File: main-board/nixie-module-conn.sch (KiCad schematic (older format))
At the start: 3 parts, among them P3 CONN_02X05, P4 CONN_02X05, U4 PCF8574

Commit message: #1 - zmiana wartosci kondensator do typuszeregu, usuniecie D2, UF4004 na D4, przyciagniecie do masy bramki Q1, bezpiecznik na wejsciu przetwornicy, gniazdo IEC C7, 100n na zasilaniu PCF8574
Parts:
- added C?: 100n, symbol C
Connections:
- wire segments 60 -> 62
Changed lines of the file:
@@
 $Descr A4 11693 8268
 encoding utf-8
-Sheet 4 4
+Sheet 3 4
 Title ""
 Date ""
@@
 Wire Wire Line
 	3550 3150 3550 2550
+$Comp
+L C C?
+U 1 1 582C0EF1
+P 4850 3000
+F 0 "C?" H 4875 3100 50  0000 L CNN
+F 1 "100n" H 4875 2900 50  0000 L CNN
+F 2 "" H 4888 2850 50  0000 C CNN
+F 3 "" H 4850 3000 50  0000 C CNN
+	1    4850 3000
+	1    0    0    -1
+$EndComp
+$Comp
+L GND #PWR?
+U 1 1 582C10A0
+P 4850 3200
+F 0 "#PWR?" H 4850 2950 50  0001 C CNN
+F 1 "GND" H 4850 3050 50  0000 C CNN
+F 2 "" H 4850 3200 50  0000 C CNN
+F 3 "" H 4850 3200 50  0000 C CNN
+	1    4850 3200
+	1    0    0    -1
+$EndComp
+Wire Wire Line
+	4850 3200 4850 3150
+Wire Wire Line
+	4850 2850 4850 2800
 $EndSCHEMATC

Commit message: #1 - stabilizator LDO AMS1117-3.3V
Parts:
- gave numbers to parts that had none: 1
- renumbered P3 to P4, P4 to P5, U4 to U5
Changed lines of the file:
@@
 $EndDescr
 $Comp
-L PCF8574 U4
+L PCF8574 U5
 U 1 1 58191F22
 P 5550 3800
-AR Path="/581979CF/58191F22" Ref="U4"  Part="1"
-AR Path="/58191DB1/58191F22" Ref="U4"  Part="1"
-F 0 "U4" H 5200 4400 50  0000 L CNN
+AR Path="/58191DB1/58191F22" Ref="U5"  Part="1"
+AR Path="/581979CF/58191F22" Ref="U6"  Part="1"
+F 0 "U5" H 5200 4400 50  0000 L CNN
 F 1 "PCF8574" H 5650 4400 50  0000 L CNN
 F 2 "" H 5550 3800 50  0000 C CNN
@@
 5VDC
 $Comp
-L VDD #PWR016
+L VDD #PWR028
 U 1 1 58192F62
 P 4850 2800
-AR Path="/581979CF/58192F62" Ref="#PWR016"  Part="1"
-AR Path="/58191DB1/58192F62" Ref="#PWR016"  Part="1"
-F 0 "#PWR016" H 4850 2650 50  0001 C CNN
+AR Path="/58191DB1/58192F62" Ref="#PWR028"  Part="1"
+AR Path="/581979CF/58192F62" Ref="#PWR033"  Part="1"
+F 0 "#PWR028" H 4850 2650 50  0001 C CNN
 F 1 "VDD" H 4850 2950 50  0000 C CNN
 F 2 "" H 4850 2800 50  0000 C CNN
@@
 $EndComp
 $Comp
-L PWR_FLAG #FLG017
+L PWR_FLAG #FLG029
 U 1 1 58192F79
 P 4150 3100
-AR Path="/581979CF/58192F79" Ref="#FLG017"  Part="1"
-AR Path="/58191DB1/58192F79" Ref="#FLG017"  Part="1"
-F 0 "#FLG017" H 4150 3195 50  0001 C CNN
+AR Path="/58191DB1/58192F79" Ref="#FLG029"  Part="1"
+AR Path="/581979CF/58192F79" Ref="#FLG034"  Part="1"
+F 0 "#FLG029" H 4150 3195 50  0001 C CNN
 F 1 "PWR_FLAG" H 4150 3280 50  0000 C CNN
 F 2 "" H 4150 3100 50  0000 C CNN
@@
 GND
 $Comp
-L PWR_FLAG #FLG018
+L PWR_FLAG #FLG030
 U 1 1 581931A2
 P 4100 4350
-AR Path="/581979CF/581931A2" Ref="#FLG018"  Part="1"
-AR Path="/58191DB1/581931A2" Ref="#FLG018"  Part="1"
-F 0 "#FLG018" H 4100 4445 50  0001 C CNN
+AR Path="/58191DB1/581931A2" Ref="#FLG030"  Part="1"
+AR Path="/581979CF/581931A2" Ref="#FLG035"  Part="1"
+F 0 "#FLG030" H 4100 4445 50  0001 C CNN
 F 1 "PWR_FLAG" H 4100 4530 50  0000 C CNN
 F 2 "" H 4100 4350 50  0000 C CNN
@@
 $EndComp
 $Comp
-L GND #PWR019
+L GND #PWR031
 U 1 1 581931CA
 P 4900 4800
-AR Path="/581979CF/581931CA" Ref="#PWR019"  Part="1"
-AR Path="/58191DB1/581931CA" Ref="#PWR019"  Part="1"
-F 0 "#PWR019" H 4900 4550 50  0001 C CNN
+AR Path="/58191DB1/581931CA" Ref="#PWR031"  Part="1"
+AR Path="/581979CF/581931CA" Ref="#PWR036"  Part="1"
+F 0 "#PWR031" H 4900 4550 50  0001 C CNN
 F 1 "GND" H 4900 4650 50  0000 C CNN
 F 2 "" H 4900 4800 50  0000 C CNN
@@
 	4600 3900 5050 3900
 $Comp
-L CONN_02X05 P3
+L CONN_02X05 P4
 U 1 1 58193880
 P 7450 3300
-AR Path="/581979CF/58193880" Ref="P3"  Part="1"
-AR Path="/58191DB1/58193880" Ref="P3"  Part="1"
-F 0 "P3" H 7450 3600 50  0000 C CNN
+AR Path="/58191DB1/58193880" Ref="P4"  Part="1"
+AR Path="/581979CF/58193880" Ref="P6"  Part="1"
+F 0 "P4" H 7450 3600 50  0000 C CNN
 F 1 "CONN_02X05" H 7450 3000 50  0000 C CNN
 F 2 "" H 7450 2100 50  0000 C CNN
@@
 $EndComp
 $Comp
-L CONN_02X05 P4
+L CONN_02X05 P5
 U 1 1 581938E3
 P 7450 4350
-AR Path="/581979CF/581938E3" Ref="P4"  Part="1"
-AR Path="/58191DB1/581938E3" Ref="P4"  Part="1"
-F 0 "P4" H 7450 4650 50  0000 C CNN
+AR Path="/58191DB1/581938E3" Ref="P5"  Part="1"
+AR Path="/581979CF/581938E3" Ref="P7"  Part="1"
+F 0 "P5" H 7450 4650 50  0000 C CNN
 F 1 "CONN_02X05" H 7450 4050 50  0000 C CNN
 F 2 "" H 7450 3150 50  0000 C CNN
@@
 	3550 3150 3550 2550
 $Comp
-L C C?
+L C C18
 U 1 1 582C0EF1
 P 4850 3000
-F 0 "C?" H 4875 3100 50  0000 L CNN
+AR Path="/58191DB1/582C0EF1" Ref="C18"  Part="1"
+AR Path="/581979CF/582C0EF1" Ref="C19"  Part="1"
+F 0 "C18" H 4875 3100 50  0000 L CNN
 F 1 "100n" H 4875 2900 50  0000 L CNN
 F 2 "" H 4888 2850 50  0000 C CNN
@@
 $EndComp
 $Comp
-L GND #PWR?
+L GND #PWR032
 U 1 1 582C10A0
 P 4850 3200
-F 0 "#PWR?" H 4850 2950 50  0001 C CNN
+AR Path="/58191DB1/582C10A0" Ref="#PWR032"  Part="1"
+AR Path="/581979CF/582C10A0" Ref="#PWR037"  Part="1"
+F 0 "#PWR032" H 4850 2950 50  0001 C CNN
 F 1 "GND" H 4850 3050 50  0000 C CNN
 F 2 "" H 4850 3200 50  0000 C CNN

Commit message: Oznaczenie MOSFET-ow od I2C; pojemnosc do filtrowania wysokich czestotliwosci za przetwornica boost; obudowy wiekszosci elementow
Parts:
- C18: footprint (none) -> Capacitors_SMD:C_0805_HandSoldering
- P4, P5: footprint (none) -> Pin_Headers:Pin_Header_Straight_SMT_02x05
- U4: renamed from U5; footprint (none) -> Housings_SOIC:SOIC-16W_7.5x10.3mm_Pitch1.27mm
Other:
- note removed: "Gowniane oznaczenie\n8pin - GND"
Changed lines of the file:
@@
 $EndDescr
 $Comp
-L PCF8574 U5
+L PCF8574 U4
 U 1 1 58191F22
 P 5550 3800
-AR Path="/58191DB1/58191F22" Ref="U5"  Part="1"
-AR Path="/581979CF/58191F22" Ref="U6"  Part="1"
-F 0 "U5" H 5200 4400 50  0000 L CNN
+AR Path="/58191DB1/58191F22" Ref="U4"  Part="1"
+AR Path="/581979CF/58191F22" Ref="U5"  Part="1"
+F 0 "U4" H 5200 4400 50  0000 L CNN
 F 1 "PCF8574" H 5650 4400 50  0000 L CNN
-F 2 "" H 5550 3800 50  0000 C CNN
+F 2 "Housings_SOIC:SOIC-16W_7.5x10.3mm_Pitch1.27mm" H 5550 3800 50  0001 C CNN
 F 3 "" H 5550 3800 50  0000 C CNN
 	1    5550 3800
@@
 5VDC
 $Comp
-L VDD #PWR028
+L VDD #PWR029
 U 1 1 58192F62
 P 4850 2800
-AR Path="/58191DB1/58192F62" Ref="#PWR028"  Part="1"
-AR Path="/581979CF/58192F62" Ref="#PWR033"  Part="1"
-F 0 "#PWR028" H 4850 2650 50  0001 C CNN
+AR Path="/58191DB1/58192F62" Ref="#PWR029"  Part="1"
+AR Path="/581979CF/58192F62" Ref="#PWR034"  Part="1"
+F 0 "#PWR034" H 4850 2650 50  0001 C CNN
 F 1 "VDD" H 4850 2950 50  0000 C CNN
 F 2 "" H 4850 2800 50  0000 C CNN
@@
 $EndComp
 $Comp
-L PWR_FLAG #FLG029
+L PWR_FLAG #FLG030
 U 1 1 58192F79
 P 4150 3100
-AR Path="/58191DB1/58192F79" Ref="#FLG029"  Part="1"
-AR Path="/581979CF/58192F79" Ref="#FLG034"  Part="1"
-F 0 "#FLG029" H 4150 3195 50  0001 C CNN
+AR Path="/58191DB1/58192F79" Ref="#FLG030"  Part="1"
+AR Path="/581979CF/58192F79" Ref="#FLG035"  Part="1"
+F 0 "#FLG035" H 4150 3195 50  0001 C CNN
 F 1 "PWR_FLAG" H 4150 3280 50  0000 C CNN
 F 2 "" H 4150 3100 50  0000 C CNN
@@
 GND
 $Comp
-L PWR_FLAG #FLG030
+L PWR_FLAG #FLG031
 U 1 1 581931A2
 P 4100 4350
-AR Path="/58191DB1/581931A2" Ref="#FLG030"  Part="1"
-AR Path="/581979CF/581931A2" Ref="#FLG035"  Part="1"
-F 0 "#FLG030" H 4100 4445 50  0001 C CNN
+AR Path="/58191DB1/581931A2" Ref="#FLG031"  Part="1"
+AR Path="/581979CF/581931A2" Ref="#FLG036"  Part="1"
+F 0 "#FLG036" H 4100 4445 50  0001 C CNN
 F 1 "PWR_FLAG" H 4100 4530 50  0000 C CNN
 F 2 "" H 4100 4350 50  0000 C CNN
@@
 $EndComp
 $Comp
-L GND #PWR031
+L GND #PWR032
 U 1 1 581931CA
 P 4900 4800
-AR Path="/58191DB1/581931CA" Ref="#PWR031"  Part="1"
-AR Path="/581979CF/581931CA" Ref="#PWR036"  Part="1"
-F 0 "#PWR031" H 4900 4550 50  0001 C CNN
+AR Path="/58191DB1/581931CA" Ref="#PWR032"  Part="1"
+AR Path="/581979CF/581931CA" Ref="#PWR037"  Part="1"
+F 0 "#PWR037" H 4900 4550 50  0001 C CNN
 F 1 "GND" H 4900 4650 50  0000 C CNN
 F 2 "" H 4900 4800 50  0000 C CNN
@@
 F 0 "P4" H 7450 3600 50  0000 C CNN
 F 1 "CONN_02X05" H 7450 3000 50  0000 C CNN
-F 2 "" H 7450 2100 50  0000 C CNN
+F 2 "Pin_Headers:Pin_Header_Straight_SMT_02x05" H 7450 2100 50  0001 C CNN
 F 3 "" H 7450 2100 50  0000 C CNN
 	1    7450 3300
@@
 F 0 "P5" H 7450 4650 50  0000 C CNN
 F 1 "CONN_02X05" H 7450 4050 50  0000 C CNN
-F 2 "" H 7450 3150 50  0000 C CNN
+F 2 "Pin_Headers:Pin_Header_Straight_SMT_02x05" H 7450 3150 50  0001 C CNN
 F 3 "" H 7450 3150 50  0000 C CNN
 	1    7450 4350
@@
 Text Label 7900 3300 2    60   ~ 0
 1D
-Text Notes 5500 4650 2    60   ~ 0
-Gowniane oznaczenie\n8pin - GND
 Text Label 7000 4250 0    60   ~ 0
 2A
@@
 F 0 "C18" H 4875 3100 50  0000 L CNN
 F 1 "100n" H 4875 2900 50  0000 L CNN
-F 2 "" H 4888 2850 50  0000 C CNN
+F 2 "Capacitors_SMD:C_0805_HandSoldering" H 4888 2850 50  0001 C CNN
 F 3 "" H 4850 3000 50  0000 C CNN
 	1    4850 3000
@@
 $EndComp
 $Comp
-L GND #PWR032
+L GND #PWR033
 U 1 1 582C10A0
 P 4850 3200
-AR Path="/58191DB1/582C10A0" Ref="#PWR032"  Part="1"
-AR Path="/581979CF/582C10A0" Ref="#PWR037"  Part="1"
-F 0 "#PWR032" H 4850 2950 50  0001 C CNN
+AR Path="/58191DB1/582C10A0" Ref="#PWR033"  Part="1"
+AR Path="/581979CF/582C10A0" Ref="#PWR038"  Part="1"
+F 0 "#PWR038" H 4850 2950 50  0001 C CNN
 F 1 "GND" H 4850 3050 50  0000 C CNN
 F 2 "" H 4850 3200 50  0000 C CNN

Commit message: usunięcie błędnego połączenia VDD z +5V
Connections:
- net labels removed: VDD
- wire segments 62 -> 60
- no-connect marks 0 -> 1
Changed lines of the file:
@@
 Text HLabel 3550 3300 0    60   Input ~ 0
 5VDC
-$Comp
-L VDD #PWR029
-U 1 1 58192F62
-P 4850 2800
-AR Path="/58191DB1/58192F62" Ref="#PWR029"  Part="1"
-AR Path="/581979CF/58192F62" Ref="#PWR034"  Part="1"
-F 0 "#PWR034" H 4850 2650 50  0001 C CNN
-F 1 "VDD" H 4850 2950 50  0000 C CNN
-F 2 "" H 4850 2800 50  0000 C CNN
-F 3 "" H 4850 2800 50  0000 C CNN
-	1    4850 2800
-	1    0    0    -1
-$EndComp
-$Comp
-L PWR_FLAG #FLG030
-U 1 1 58192F79
-P 4150 3100
-AR Path="/58191DB1/58192F79" Ref="#FLG030"  Part="1"
-AR Path="/581979CF/58192F79" Ref="#FLG035"  Part="1"
-F 0 "#FLG035" H 4150 3195 50  0001 C CNN
-F 1 "PWR_FLAG" H 4150 3280 50  0000 C CNN
-F 2 "" H 4150 3100 50  0000 C CNN
-F 3 "" H 4150 3100 50  0000 C CNN
-	1    4150 3100
-	0    1    1    0
-$EndComp
-Wire Wire Line
-	3850 3100 4150 3100
 Wire Wire Line
 	3850 2800 6800 2800
@@
 Wire Wire Line
 	3850 2800 3850 3300
-Connection ~ 3850 3100
 Text HLabel 3550 4200 0    60   Input ~ 0
 GND
 $Comp
-L PWR_FLAG #FLG031
-U 1 1 581931A2
-P 4100 4350
-AR Path="/58191DB1/581931A2" Ref="#FLG031"  Part="1"
-AR Path="/581979CF/581931A2" Ref="#FLG036"  Part="1"
-F 0 "#FLG036" H 4100 4445 50  0001 C CNN
-F 1 "PWR_FLAG" H 4100 4530 50  0000 C CNN
-F 2 "" H 4100 4350 50  0000 C CNN
-F 3 "" H 4100 4350 50  0000 C CNN
-	1    4100 4350
-	0    1    1    0
-$EndComp
-$Comp
-L GND #PWR032
+L GND #PWR027
 U 1 1 581931CA
 P 4900 4800
-AR Path="/58191DB1/581931CA" Ref="#PWR032"  Part="1"
-AR Path="/581979CF/581931CA" Ref="#PWR037"  Part="1"
-F 0 "#PWR037" H 4900 4550 50  0001 C CNN
+AR Path="/58191DB1/581931CA" Ref="#PWR027"  Part="1"
+AR Path="/581979CF/581931CA" Ref="#PWR030"  Part="1"
+F 0 "#PWR027" H 4900 4550 50  0001 C CNN
 F 1 "GND" H 4900 4650 50  0000 C CNN
 F 2 "" H 4900 4800 50  0000 C CNN
@@
 $EndComp
 Wire Wire Line
-	3850 4350 4100 4350
-Wire Wire Line
 	3850 4200 3850 4700
 Wire Wire Line
@@
 Wire Wire Line
 	4900 4700 4900 4800
-Connection ~ 3850 4350
 Wire Wire Line
 	5550 4700 5550 4500
@@
 $EndComp
 $Comp
-L GND #PWR033
+L GND #PWR028
 U 1 1 582C10A0
 P 4850 3200
-AR Path="/58191DB1/582C10A0" Ref="#PWR033"  Part="1"
-AR Path="/581979CF/582C10A0" Ref="#PWR038"  Part="1"
-F 0 "#PWR038" H 4850 2950 50  0001 C CNN
+AR Path="/58191DB1/582C10A0" Ref="#PWR028"  Part="1"
+AR Path="/581979CF/582C10A0" Ref="#PWR031"  Part="1"
+F 0 "#PWR028" H 4850 2950 50  0001 C CNN
 F 1 "GND" H 4850 3050 50  0000 C CNN
 F 2 "" H 4850 3200 50  0000 C CNN
@@
 Wire Wire Line
 	4850 2850 4850 2800
+NoConn ~ 5050 4200
 $EndSCHEMATC

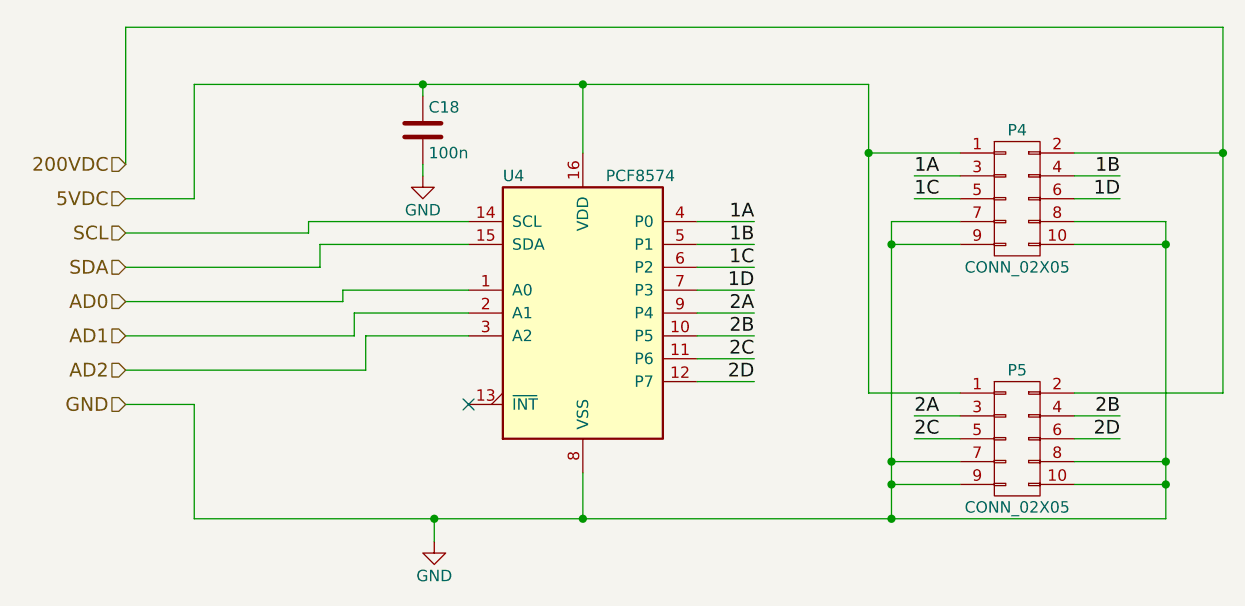
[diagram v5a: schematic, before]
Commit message: Obrys plytki 40% elementow
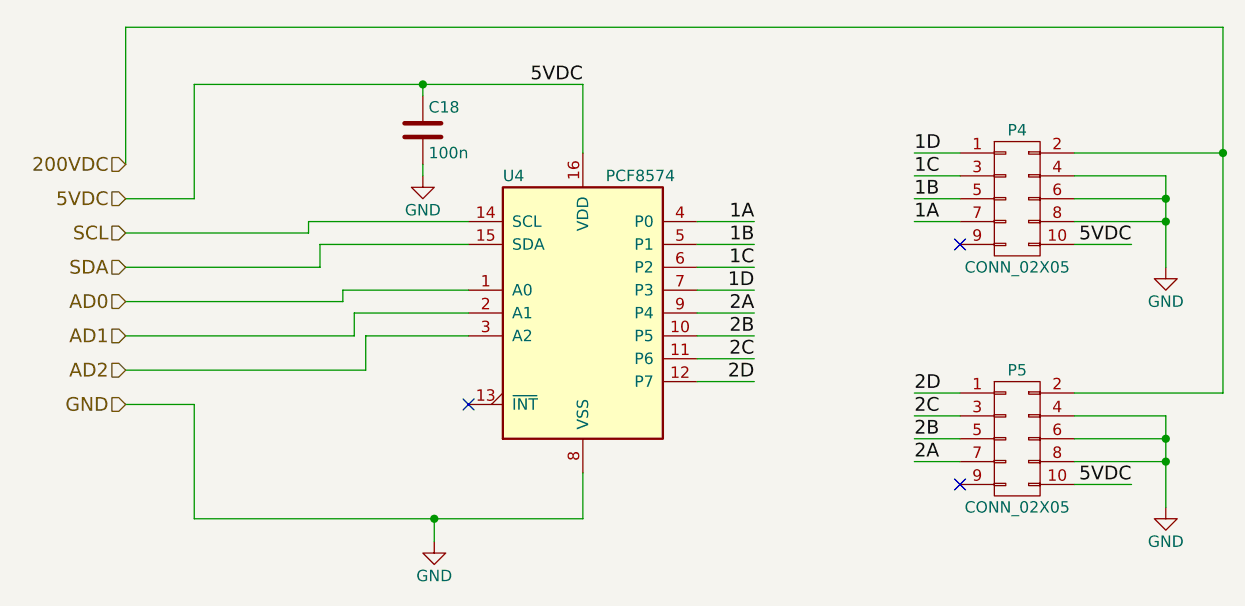
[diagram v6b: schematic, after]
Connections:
- net 1A: now also P4.7 (P7); no longer P4.3 (P3)
- net 1B: now also P4.5 (P5); no longer P4.4 (P4)
- net 1C: now also P4.3 (P3); no longer P4.5 (P5)
- net 1D: now also P4.1 (P1); no longer P4.6 (P6)
- net 2A: now also P5.7 (P7); no longer P5.3 (P3)
- net 2B: now also P5.5 (P5); no longer P5.4 (P4)
- net 2C: now also P5.3 (P3); no longer P5.5 (P5)
- net 2D: now also P5.1 (P1); no longer P5.6 (P6)
- net 5VDC: now also P4.10 (P10), P5.10 (P10); no longer P4.1 (P1), P5.1 (P1)
- net GND: now also P4.4 (P4), P4.6 (P6), P5.4 (P4), P5.6 (P6); no longer P4.10 (P10), P4.7 (P7), P4.9 (P9), P5.10 (P10), P5.7 (P7), P5.9 (P9)
- no-connect marks 1 -> 3
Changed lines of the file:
@@
 5VDC
-Wire Wire Line
-	3850 2800 6800 2800
 Wire Wire Line
 	5550 2800 5550 3100
-Connection ~ 4850 2800
 Wire Wire Line
 	3850 2800 3850 3300
@@
 GND
 $Comp
-L GND #PWR027
+L GND #PWR026
 U 1 1 581931CA
 P 4900 4800
-AR Path="/58191DB1/581931CA" Ref="#PWR027"  Part="1"
+AR Path="/58191DB1/581931CA" Ref="#PWR026"  Part="1"
 AR Path="/581979CF/581931CA" Ref="#PWR030"  Part="1"
-F 0 "#PWR027" H 4900 4550 50  0001 C CNN
+F 0 "#PWR030" H 4900 4550 50  0001 C CNN
 F 1 "GND" H 4900 4650 50  0000 C CNN
 F 2 "" H 4900 4800 50  0000 C CNN
@@
 	3850 4200 3850 4700
 Wire Wire Line
-	3850 4700 8100 4700
-Wire Wire Line
 	4900 4700 4900 4800
-Wire Wire Line
-	5550 4700 5550 4500
-Connection ~ 4900 4700
 Wire Wire Line
 	3850 3300 3550 3300
@@
 $EndComp
 Wire Wire Line
-	6800 2800 6800 4150
-Wire Wire Line
-	6800 3100 7200 3100
-Connection ~ 5550 2800
-Wire Wire Line
-	6800 4150 7200 4150
-Connection ~ 6800 3100
-Wire Wire Line
-	6900 3400 6900 4700
-Wire Wire Line
-	6900 4550 7200 4550
-Connection ~ 5550 4700
-Wire Wire Line
-	6900 4450 7200 4450
-Connection ~ 6900 4550
-Wire Wire Line
-	8100 4700 8100 3400
+	8100 3200 8100 3600
 Wire Wire Line
 	8100 4450 7700 4450
-Connection ~ 6900 4700
-Wire Wire Line
-	7700 4550 8100 4550
-Connection ~ 8100 4550
-Wire Wire Line
-	6900 3500 7200 3500
-Connection ~ 6900 4450
-Wire Wire Line
-	6900 3400 7200 3400
-Connection ~ 6900 3500
-Wire Wire Line
-	8100 3500 7700 3500
-Connection ~ 8100 4450
 Wire Wire Line
 	8100 3400 7700 3400
-Connection ~ 8100 3500
 Wire Wire Line
 	6050 3400 6300 3400
@@
 2D
 Wire Wire Line
-	7000 3200 7200 3200
-Wire Wire Line
 	7000 3300 7200 3300
 Wire Wire Line
-	7900 3200 7700 3200
-Wire Wire Line
-	7900 3300 7700 3300
-Wire Wire Line
-	7000 4250 7200 4250
+	8100 3200 7700 3200
+Wire Wire Line
+	8100 3300 7700 3300
 Wire Wire Line
 	7000 4350 7200 4350
 Wire Wire Line
-	7900 4250 7700 4250
-Wire Wire Line
-	7900 4350 7700 4350
+	7700 4250 8100 4250
+Wire Wire Line
+	7700 4350 8100 4350
+Text Label 7000 3400 0    60   ~ 0
+1A
+Text Label 7000 3300 0    60   ~ 0
+1B
 Text Label 7000 3200 0    60   ~ 0
-1A
-Text Label 7900 3200 2    60   ~ 0
-1B
-Text Label 7000 3300 0    60   ~ 0
 1C
-Text Label 7900 3300 2    60   ~ 0
+Text Label 7000 3100 0    60   ~ 0
 1D
+Text Label 7000 4450 0    60   ~ 0
+2A
+Text Label 7000 4350 0    60   ~ 0
+2B
 Text Label 7000 4250 0    60   ~ 0
-2A
-Text Label 7900 4250 2    60   ~ 0
-2B
-Text Label 7000 4350 0    60   ~ 0
 2C
-Text Label 7900 4350 2    60   ~ 0
+Text Label 7000 4150 0    60   ~ 0
 2D
 Text HLabel 3550 3150 0    60   Input ~ 0
@@
 $EndComp
 $Comp
-L GND #PWR028
+L GND #PWR027
 U 1 1 582C10A0
 P 4850 3200
-AR Path="/58191DB1/582C10A0" Ref="#PWR028"  Part="1"
+AR Path="/58191DB1/582C10A0" Ref="#PWR027"  Part="1"
 AR Path="/581979CF/582C10A0" Ref="#PWR031"  Part="1"
-F 0 "#PWR028" H 4850 2950 50  0001 C CNN
+F 0 "#PWR031" H 4850 2950 50  0001 C CNN
 F 1 "GND" H 4850 3050 50  0000 C CNN
 F 2 "" H 4850 3200 50  0000 C CNN
@@
 	4850 2850 4850 2800
 NoConn ~ 5050 4200
+Wire Wire Line
+	7200 4450 7000 4450
+Connection ~ 8100 4350
+Connection ~ 8100 3300
+Wire Wire Line
+	7000 3400 7200 3400
+Wire Wire Line
+	7000 3100 7200 3100
+Wire Wire Line
+	7000 4150 7200 4150
+Wire Wire Line
+	7950 3500 7700 3500
+Wire Wire Line
+	7950 4550 7700 4550
+Wire Wire Line
+	3850 2800 5550 2800
+Connection ~ 4850 2800
+Text Label 5550 2800 2    60   ~ 0
+5VDC
+Text Label 7950 4550 2    60   ~ 0
+5VDC
+Text Label 7950 3500 2    60   ~ 0
+5VDC
+Wire Wire Line
+	5550 4700 5550 4500
+Wire Wire Line
+	3850 4700 5550 4700
+Connection ~ 4900 4700
+Wire Wire Line
+	8100 4250 8100 4650
+$Comp
+L GND #PWR028
+U 1 1 5851458D
+P 8100 3600
+AR Path="/58191DB1/5851458D" Ref="#PWR028"  Part="1"
+AR Path="/581979CF/5851458D" Ref="#PWR032"  Part="1"
+F 0 "#PWR032" H 8100 3350 50  0001 C CNN
+F 1 "GND" H 8100 3450 50  0000 C CNN
+F 2 "" H 8100 3600 50  0000 C CNN
+F 3 "" H 8100 3600 50  0000 C CNN
+	1    8100 3600
+	1    0    0    -1
+$EndComp
+$Comp
+L GND #PWR029
+U 1 1 585145AB
+P 8100 4650
+AR Path="/58191DB1/585145AB" Ref="#PWR029"  Part="1"
+AR Path="/581979CF/585145AB" Ref="#PWR033"  Part="1"
+F 0 "#PWR033" H 8100 4400 50  0001 C CNN
+F 1 "GND" H 8100 4500 50  0000 C CNN
+F 2 "" H 8100 4650 50  0000 C CNN
+F 3 "" H 8100 4650 50  0000 C CNN
+	1    8100 4650
+	1    0    0    -1
+$EndComp
+Connection ~ 8100 4450
+Connection ~ 8100 3400
+Wire Wire Line
+	7000 3200 7200 3200
+NoConn ~ 7200 3500
+Wire Wire Line
+	7000 4250 7200 4250
+NoConn ~ 7200 4550
 $EndSCHEMATC
